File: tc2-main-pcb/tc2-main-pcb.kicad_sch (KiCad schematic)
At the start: 70 parts, among them J3 Conn_02x04_Odd_Even, SW2 K2-6639SP-M4SC-04, U1 ATtiny1616-M, U2 W25Q128JVS, U3 RP2040, U4 MT29F2G01ABAGDWB-IT, U5 SHT30-DIS, U6 PCF8563T, Y1 Crystal_GND24, Y2 Crystal

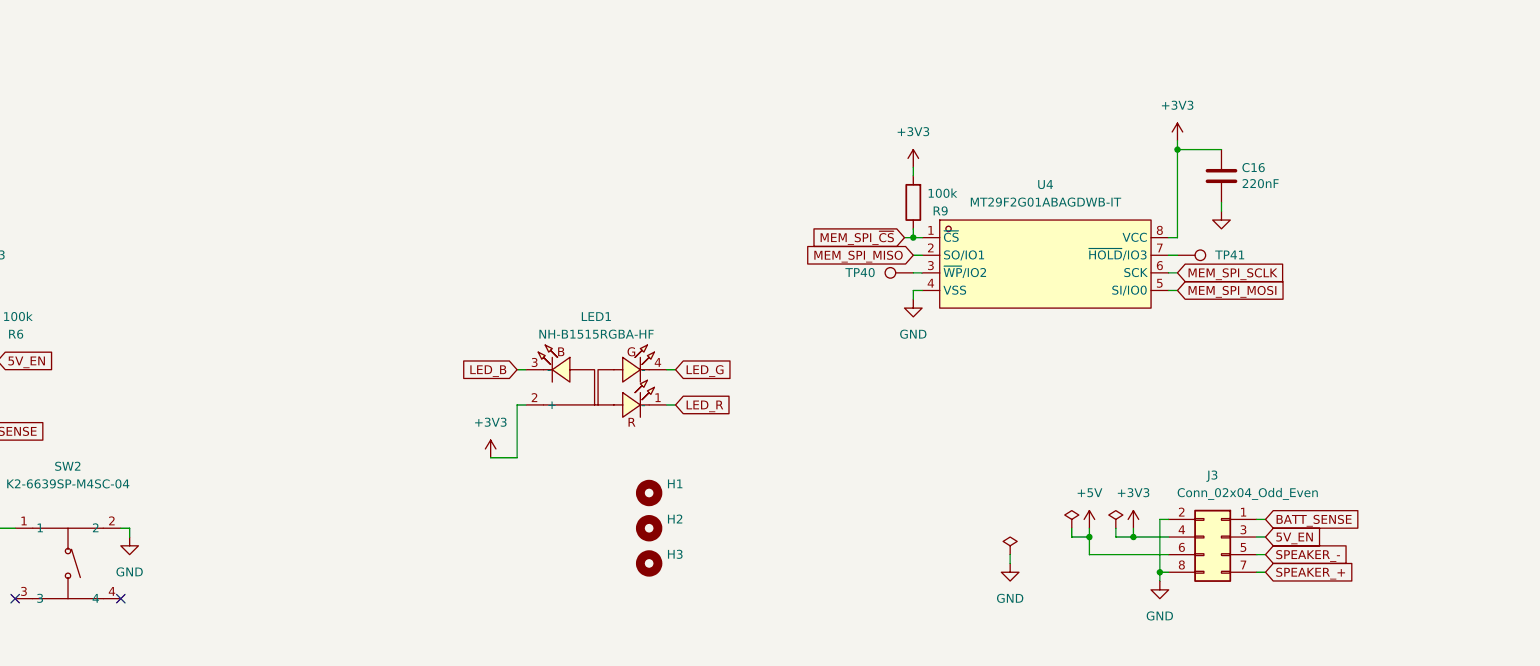
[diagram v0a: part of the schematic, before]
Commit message: Clean up of files and updated drawings for PCBs
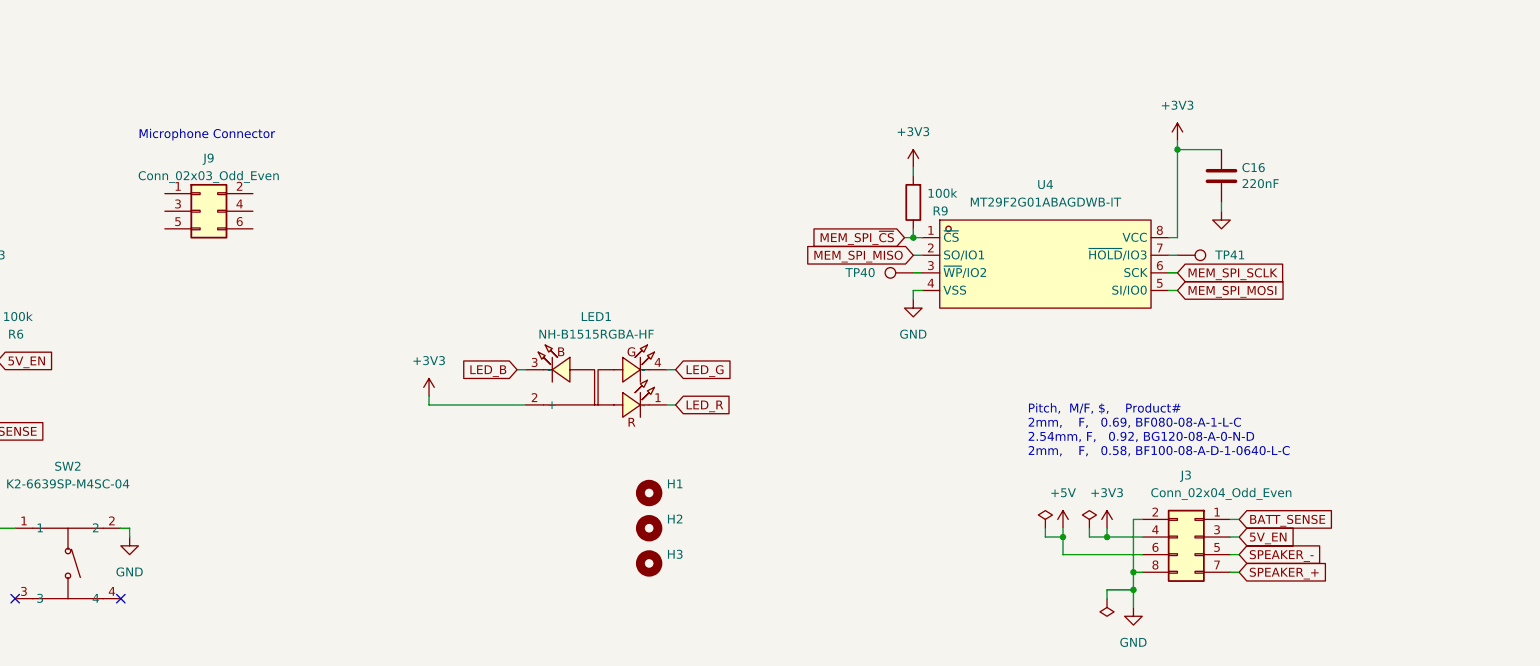
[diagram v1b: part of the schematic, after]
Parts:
- added J9: Conn_02x03_Odd_Even, cacophony-library:mic-pcb, symbol Connector_Generic:Conn_02x03_Odd_Even
- J3: footprint cacophony-library:power-pcb -> cacophony-library:power-pcb-3; Digikey (none) -> BF100-08-A-D-1-0640-L-C
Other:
- note added: "Microphone Connector"
- note added: "Pitch, M/F, $, Product# 2mm, F, 0.69, BF080-08-A-1-L-C 2.54mm, F, 0.92, BG120-08-A-0-N-D 2mm, F, 0.58, BF100-08-A-D-1-0640-L-C"
- moved on the sheet: J3

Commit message: Version 2 WIP
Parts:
- removed TP10, TP11, TP4: TestPoint, cacophony-library:TP, symbol Connector:TestPoint
- added H4: MountingHole, cacophony-library:Mouning_Hole_M3, symbol Mechanical:MountingHole
- added H5, H6: MountingHole, MountingHole:MountingHole_2.2mm_M2, symbol Mechanical:MountingHole
- added R34: 22ohm, Resistor_SMD:R_0402_1005Metric, symbol Device:R
- added R35: 100k, Resistor_SMD:R_0402_1005Metric, symbol Device:R
- added TP18, TP19, TP20: TestPoint, cacophony-library:TP, symbol Connector:TestPoint
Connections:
- net +3V3: now also J9.4 (Pin_4), R35.1
- net BATT_SENSE: now also U1.9 (PB5); no longer U1.15 (PC0)
- net GND: now also J9.2 (Pin_2), J9.3 (Pin_3), J9.6 (Pin_6), TP14.1, TP18.1, TP19.1, TP20.1
- net LEPTON_CLK_EN: now also U3.39 (GPIO27_ADC1); no longer U3.41 (GPIO29_ADC3)
- net LEPTON_PWR_DWN_L: now also U3.40 (GPIO28_ADC2); no longer U3.39 (GPIO27_ADC1)
- net LEPTON_RESET_L: now also U3.41 (GPIO29_ADC3); no longer U3.40 (GPIO28_ADC2)
- net RTC_BT_SENSE: now also U1.10 (PB4); no longer U1.7 (PA6)
- net SPEAKER_+: now also J3.5 (Pin_5); no longer J3.7 (Pin_7)
- net SPEAKER_-: now also J3.7 (Pin_7); no longer J3.5 (Pin_5)
- net at R3.1: now also U1.5 (PA4); no longer U1.2 (PA3)
- net at TP6.1: now also U1.8 (PA7); no longer U1.10 (PB4)
- net ~{WAKEUP_PING}: now reaches U1.12 (PB2)
- net ~{WAKEUP_PING}: now also U3.6 (GPIO4), R35.2
- net at R4.1: now also U1.2 (PA3); no longer U1.5 (PA4)
- net at SW2.1: now also U1.7 (PA6); no longer U1.8 (PA7)
- net at TP7.1: now also U1.15 (PC0); no longer U1.9 (PB5)
- net GPIO16: now reaches TP26.1, U3.27 (GPIO16)
- net GPIO3: now reaches TP13.1, U3.5 (GPIO3)
- net PDM_DATA: now reaches U3.2 (GPIO0)
- net PDM_DATA: now also J9.5 (Pin_5)
- net GPIO17: now reaches TP27.1, U3.28 (GPIO17)
- net PDM_CLOCK_: now reaches U3.3 (GPIO1)
- net PDM_CLOCK_: now also R34.1
- net PDM_CLOCK: now reaches J9.1 (Pin_1)
- net PDM_CLOCK: now also R34.2
- net GPIO2: now reaches TP12.1, U3.4 (GPIO2)
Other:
- note added: "TODO Add wakeup pin connecting ATtiny, RP2040, and RPi pulled up to 3.3V. Add wake up pin from ATtiny to RP2040."
- note added: "Test ground points."
- note removed: "Replace ATTiny, RTC with STM32 and Touch sensor"
- moved on the sheet: J9, R3, R4, SW2, TP12, TP13, TP26, TP27, TP6, TP7

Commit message: Thermal camera V2 WIP
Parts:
- J3: LCSC C124386 -> (none)
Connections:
- net SPEAKER_+: now also J3.7 (Pin_7); no longer J3.5 (Pin_5)
- net SPEAKER_-: now also J3.5 (Pin_5); no longer J3.7 (Pin_7)
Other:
- note added: "Pitch, M/F, $, Product# 2mm, F, 0.69, BF080-08-A-1-L-C 2.54mm, F, 0.92, BG120-08-A-0-N-D 2mm, F, 0.58, BF100-08-A-D-1-0640-L-C Old part C124386"
- note removed: "Pitch, M/F, $, Product# 2mm, F, 0.69, BF080-08-A-1-L-C 2.54mm, F, 0.92, BG120-08-A-0-N-D 2mm, F, 0.58, BF100-08-A-D-1-0640-L-C"
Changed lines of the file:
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@@
     (effects (font (size 1.27 1.27)) (justify left bottom))
   )
-  (text "Pitch,  M/F, $,    Product#\n2mm,    F,   0.69, BF080-08-A-1-L-C\n2.54mm, F,   0.92, BG120-08-A-0-N-D\n2mm,    F,   0.58, BF100-08-A-D-1-0640-L-C\n"
+  (text "Pitch,  M/F, $,    Product#\n2mm,    F,   0.69, BF080-08-A-1-L-C\n2.54mm, F,   0.92, BG120-08-A-0-N-D\n2mm,    F,   0.58, BF100-08-A-D-1-0640-L-C\n\nOld part C124386\n"
     (at 242.57 254 0)
     (effects (font (face "RobotoMono Nerd Font Mono") (size 1.27 1.27)) (justify left bottom))
@@
     )
   )
-  (global_label "SPEAKER_-" (shape input) (at 273.05 270.51 0) (fields_autoplaced)
+  (global_label "SPEAKER_-" (shape input) (at 273.05 267.97 0) (fields_autoplaced)
     (effects (font (size 1.27 1.27)) (justify left))
-    (property "Intersheetrefs" "${INTERSHEET_REFS}" (at 286.4093 270.4306 0)
+    (property "Intersheetrefs" "${INTERSHEET_REFS}" (at 286.4093 267.8906 0)
       (effects (font (size 1.27 1.27)) (justify left) hide)
     )
@@
     )
   )
-  (global_label "SPEAKER_+" (shape input) (at 273.05 267.97 0) (fields_autoplaced)
+  (global_label "SPEAKER_+" (shape input) (at 273.05 270.51 0) (fields_autoplaced)
     (effects (font (size 1.27 1.27)) (justify left))
-    (property "Intersheetrefs" "${INTERSHEET_REFS}" (at 286.4093 267.8906 0)
+    (property "Intersheetrefs" "${INTERSHEET_REFS}" (at 286.4093 270.4306 0)
       (effects (font (size 1.27 1.27)) (justify left) hide)
     )
@@
       (effects (font (size 1.27 1.27)) hide)
     )
-    (property "LCSC" "C124386" (at 266.7 265.43 0)
+    (property "LCSC" "" (at 266.7 265.43 0)
       (effects (font (size 1.27 1.27)) hide)
     )

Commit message: P2 milestone
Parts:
- removed C17: 220nF, Capacitor_SMD:C_0402_1005Metric, symbol Device:C_Small
- removed H2: MountingHole, cacophony-library:Mouning_Hole_M3, symbol Mechanical:MountingHole
- removed J3: Conn_02x04_Odd_Even, cacophony-library:power-pcb-3, symbol Connector_Generic:Conn_02x04_Odd_Even
- removed TP15, TP16, TP2, TP3, TP44, TP5, TP6, TP7, TP8: TestPoint, cacophony-library:TP, symbol Connector:TestPoint
- removed U5: SHT30-DIS, Sensor_Humidity:Sensirion_DFN-8-1EP_2.5x2.5mm_P0.5mm_EP1.1x1.7mm, symbol Sensor_Humidity:SHT30-DIS
- added C17: 1u, Capacitor_SMD:C_0402_1005Metric, symbol Device:C
- added C38, C39, C43: 10uF, Capacitor_SMD:C_0603_1608Metric, symbol Device:C_Small
- added J10: Conn_02x06_Odd_Even, cacophony-library:power-pcb-3.1, symbol Connector_Generic:Conn_02x06_Odd_Even
- added J2: Conn_01x03, Connector_PinHeader_2.54mm:PinHeader_1x03_P2.54mm_Vertical, symbol Connector_Generic:Conn_01x03
- added J3: Conn_01x03, cacophony-library:JST_SH_BM03B-SRSS-TB_1x03-1MP_P1.00mm_Vertical, symbol cacophony-library:Conn_01x03_MP
- added Q1: Q_PMOS_GSD, Package_TO_SOT_SMD:SOT-23, symbol Device:Q_PMOS_GSD
- added R15, R38: 100k, Resistor_SMD:R_0402_1005Metric, symbol Device:R
- added R39: 180R, Resistor_SMD:R_0402_1005Metric, symbol Device:R
- added TP28, TP6: TestPoint_2Pole, cacophony-library:test-point-2p, symbol Connector:TestPoint_2Pole
- added U13: AHT21, cacophony-library:SENSOR-SMD_L3.0-W3.0-P1.00-BR, symbol cacophony-library:AHT21
- H1, H3, H4, H5, H6, TP1, TP12, TP13, TP14, TP17, TP18, TP19, TP20, TP26, TP27, TP40, TP41, TP46, TP47, TP9: now left out of the parts list
- SW2: footprint cacophony-library:KEY-SMD_4P-L6.0-W6.0-P3.90-LS9.0 -> cacophony-library:KEY-SMD_4P-L6.0-W6.0-P3.90_K2-6639SP-K4SC-04; symbol cacophony-library:K2-6639SP-M4SC-04 -> cacophony-library:K2-6639SP-O4SC-04; LCSC Part C149500 -> C223734
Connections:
- net +3V3: now also C17.1, C43.1, J10.3 (Pin_3), Q1.2 (S), R38.2, R39.1; no longer C10.1, C11.1, C12.1, C13.1, C14.1, C15.1, C16.1, C2.1, C8.1, C9.1, R2.1, R9.2, U2.8 (VCC), U3.1 (IOVDD), U3.10 (IOVDD), U3.22 (IOVDD), U3.33 (IOVDD), U3.42 (IOVDD), U3.43 (ADC_AVDD), U3.44 (VREG_IN), U3.48 (USB_VDD), U3.49 (IOVDD), U4.8 (VCC)
- net +5V: now also J10.5 (Pin_5), TP28.2
- net 5V_EN: now also J10.4 (Pin_4)
- net BATT_SENSE: now also J10.2 (Pin_2)
- net GND: now also SW2.4, C17.2, C38.2, C39.2, C43.2, J10.1 (Pin_1), J10.7 (Pin_7), J2.2 (Pin_2), J3.2 (Pin_2), TP28.1, TP6.1, U13.5 (GND); no longer SW2.2
- net SCL: now also U13.3 (SCL)
- net SDA: now also U13.4 (SDA)
- net SPEAKER_+: now also J10.6 (Pin_6)
- net SPEAKER_-: now also J10.8 (Pin_8)
- net SWD: now also J2.3 (Pin_3), J3.3 (Pin_3)
- net SW_CLK: now also J2.1 (Pin_1), J3.1 (Pin_1)
- net ~{WAKEUP_PING}: now also U1.15 (PC0); no longer U1.12 (PB2)
- net ~{EN_RP2040_POWER}: now reaches U1.20 (PA1)
- net ~{EN_RP2040_POWER}: now also Q1.1 (G), R38.1
- net at TP1.1: now also U1.18 (PC3); no longer U1.17 (PC2)
- net ATTINY_RX: now reaches U1.11 (PB3)
- net ~{PI_SHUTDOWN}: now reaches U1.8 (PA7)
- new net: R15.2, U1.12 (PB2)
- new net: C39.1, R39.2, U13.2 (VDD)
- new net +3V3_rp2040: C10.1, C11.1, C12.1, C13.1, C14.1, C15.1, C16.1, C2.1, C38.1, C8.1, C9.1, Q1.3 (D), R2.1, R9.2, TP6.2, U2.8 (VCC), U3.1 (IOVDD), U3.10 (IOVDD), U3.22 (IOVDD), U3.33 (IOVDD), U3.42 (IOVDD), U3.43 (ADC_AVDD), U3.44 (VREG_IN), U3.48 (USB_VDD), U3.49 (IOVDD), U4.8 (VCC)
- new net ATTINY_TX: R15.1
- new net EN_PERIPH_POWER: J10.11 (Pin_11), U1.17 (PC2)
- new net OUT_RX: J10.12 (Pin_12)
- new net OUT_TX: J10.10 (Pin_10)
- no-connect marks 2 -> 7
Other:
- note added: "C160389"
- note removed: "TODO Add wakeup pin connecting ATtiny, RP2040, and RPi pulled up to 3.3V. Add wake up pin from ATtiny to RP2040."
- moved on the sheet: C16, H5, H6, J9, R10, R11, R35, R6, R9, TP14, TP18, TP19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

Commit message: P3-Nov release
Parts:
- removed C1: 220nF, Capacitor_SMD:C_0402_1005Metric, symbol Device:C_Small
- removed J2: Conn_01x03, Connector_PinHeader_2.54mm:PinHeader_1x03_P2.54mm_Vertical, symbol Connector_Generic:Conn_01x03
- removed LED1: NH-B1515RGBA-HF, cacophony-library:LED-ARRAY-SMD_4P-L1.6-W1.5-TL_NH-B1515RGBA, symbol cacophony-library:NH-B1515RGBA-HF
- removed R15, R35, R6: 100k, Resistor_SMD:R_0402_1005Metric, symbol Device:R
- removed R3, R4, R5: 180R, Resistor_SMD:R_0402_1005Metric, symbol Device:R
- removed SW2: K2-6639SP-M4SC-04, cacophony-library:KEY-SMD_4P-L6.0-W6.0-P3.90_K2-6639SP-K4SC-04, symbol cacophony-library:K2-6639SP-O4SC-04
- removed TP1: TestPoint, cacophony-library:TP, symbol Connector:TestPoint
- removed TP28, TP6: TestPoint_2Pole, cacophony-library:test-point-2p, symbol Connector:TestPoint_2Pole
- removed U1: ATtiny1616-M, Package_DFN_QFN:VQFN-20-1EP_3x3mm_P0.4mm_EP1.7x1.7mm, symbol MCU_Microchip_ATtiny:ATtiny1616-M
- added C33 (x4): 22uF, Capacitor_SMD:C_0603_1608Metric, symbol Device:C_Small
- added C48: 220nF, Capacitor_SMD:C_0402_1005Metric, symbol Device:C_Small
- added TP10, TP3, TP6: TP_2P, cacophony-library:test-point-2p, symbol cacophony-library:TestPoint_2Pole
- added U16: M24C02-WMN, Package_SO:SOIC-8_3.9x4.9mm_P1.27mm, symbol Memory_EEPROM:M24C02-WMN
- H1, H3, H4: footprint cacophony-library:Mouning_Hole_M3 -> cacophony-library:MountingHole_3.2mm_M3
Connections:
- net BATT_SENSE is gone; now on net OUT_RX: J10.2 (Pin_2)
- net +3V3: now also J10.10 (Pin_10), C33.1, C33.1, C48.2, TP6.2, U16.8 (VCC); no longer J10.3 (Pin_3)
- net +3V3_rp2040: now also TP3.2
- net +5V: now also J10.8 (Pin_8), C33.1, C33.1, TP10.2; no longer J10.5 (Pin_5)
- net 5V_EN: now also J10.1 (Pin_1); no longer J10.4 (Pin_4)
- net GND: now also J10.12 (Pin_12), J10.6 (Pin_6), C33.2, C33.2, C33.2, C33.2, C48.1, TP10.1, TP3.1, TP6.1, U16.4 (VSS); no longer J10.1 (Pin_1), J10.7 (Pin_7)
- net OUT_RX: no longer J10.12 (Pin_12)
- net OUT_TX: now also J10.4 (Pin_4); no longer J10.10 (Pin_10)
- net SCL: now also U16.5 (SDA)
- net SDA: now also U16.6 (SCL)
- net SPEAKER_+: now also J10.9 (Pin_9); no longer J10.6 (Pin_6)
- net SPEAKER_-: now also J10.7 (Pin_7); no longer J10.8 (Pin_8)
- net RTC_OSCO: now reaches U6.2 (OSCO), Y2.1
- net RTC_OSCI: now reaches U6.1 (OSCI), Y2.2
- net RTC_VDD: now reaches C18.1, D3.1 (K), R8.1, U6.8 (VDD)
- net RTC_BATTERY: now reaches BT1.1 (+), R7.1, R8.2
- net RTC_CLKO: now reaches TP17.1, U6.7 (CLKO)
- net AHT21_VDD: now reaches C39.1, R39.2, U13.2 (VDD)
- net MEM_~{WP}/IO2: now reaches TP40.1, U4.3 (~{WP}/IO2)
- net MEM_~{HOLD}/IO3: now reaches TP41.1, U4.7 (~{HOLD}/IO3)
- net PDM_CLOCK_ renamed PDM_CLOCK_PHY
- net RTC_BT_SENSE renamed RTC_BT_SENSE_PHY
- net ~{WAKEUP_PING} renamed ~{READ_ATTINY_CMD_REG}
- new net BATT_SENSE_HV: J10.3 (Pin_3)
- new net BATT_SENSE_LV: J10.5 (Pin_5)
- no-connect marks 7 -> 8
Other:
- added sheet ATtiny1616 (attiny1616.kicad_sch)
- note added: "Always double check allignemnt with plug PCB"
- moved on the sheet: BT1, C18, D2, D3, H1, H3, H4, J10, R34, R7, R8, TP12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

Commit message: v0.4.0
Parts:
- removed TP13, TP46, TP47, TP9: TestPoint, cacophony-library:TP, symbol Connector:TestPoint
- added C61, C63: 22pF, Capacitor_SMD:C_0402_1005Metric, symbol Device:C_Small
- added H2: MountingHole, cacophony-library:MountingHole_3.2mm_M3, symbol Mechanical:MountingHole
- added J12: USB_B_Micro, cacophony-library:MICRO-USB-TH_MICRO-USB-A14, symbol Connector:USB_B_Micro
- added R48, R50, R51: 22ohm, Resistor_SMD:R_0402_1005Metric, symbol Device:R
- added TP13: TP_2P, cacophony-library:test-point-2p, symbol cacophony-library:TestPoint_2Pole
- C62, C64, C65, C66: renamed from C33; LCSC C2980159 -> C86295
- H5, H6: footprint MountingHole:MountingHole_2.2mm_M2 -> cacophony-library:MountingHole_2.2mm_M2
- J10: LCSC (none) -> C6470934
- TP10, TP3, TP6: now left out of the parts list
- U13: value AHT21 -> AHT20_C2757850; symbol cacophony-library:AHT21 -> cacophony-library:AHT20_C2757850; LCSC (none) -> C2757850; LCSC Part C2827328 -> (none)
- U4: LCSC (none) -> C410863; LCSC Part C410863 -> (none)
- U6: footprint Package_SO:SOIC-8_3.9x4.9mm_P1.27mm -> cacophony-library:SOIC-8_3.9x4.9mm_P1.27mm
- renumbered R34 to R28
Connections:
- net GND: now also C61.2, C63.2, J12.5 (GND), J12.6 (Shield), TP13.1
- net RPI_SPI_MISO: now also R48.2; no longer U3.18 (GPIO15)
- net RTC_BATTERY: now also TP13.2
- net RTC_OSCI: now also C63.1
- net RTC_OSCO: now also C61.1
- net SCL: now also U16.6 (SCL); no longer U16.5 (SDA)
- net SDA: now also U16.5 (SDA); no longer U16.6 (SCL)
- net USB_D+: now also J12.3 (D+), R50.2; no longer U3.47 (USB_DP)
- net USB_D-: now also J12.2 (D-), R51.2; no longer U3.46 (USB_DM)
- net GPIO3 renamed I2C_BUS_LOCK
- new net RPI_SPI_MISO_PHY: R48.1, U3.18 (GPIO15)
- new net USB_D+_PHY: R50.1, U3.47 (USB_DP)
- new net USB_D-_PHY: R51.1, U3.46 (USB_DM)
- no-connect marks 8 -> 10
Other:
- note added: "I2C Address 0x38"
- note added: "I2C Address 0x51"
- note removed: "Pitch, M/F, $, Product# 2mm, F, 0.69, BF080-08-A-1-L-C 2.54mm, F, 0.92, BG120-08-A-0-N-D 2mm, F, 0.58, BF100-08-A-D-1-0640-L-C Old part C124386"
- moved on the sheet: BT1, C48, D2, R28, R7, TP26, TP27, U16

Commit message: Small update for v0.4.1
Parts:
- added R53: 1k, Resistor_SMD:R_0402_1005Metric, symbol Device:R
- BT1: LCSC (none) -> C80909
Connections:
- net I2C_BUS_LOCK: now also R53.1; no longer U3.5 (GPIO3)
- new net I2C_BUS_LOCK_PHY: R53.2, U3.5 (GPIO3)
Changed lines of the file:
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@@
 	(wire
 		(pts
+			(xy 240.03 96.52) (xy 246.38 96.52)
+		)
+		(stroke
+			(width 0)
+			(type default)
+		)
+	)
+	(wire
+		(pts
 			(xy 125.73 260.35) (xy 125.73 261.62)
 		)
@@
 	(wire
 		(pts
-			(xy 207.01 93.98) (xy 231.14 93.98)
+			(xy 207.01 93.98) (xy 215.9 93.98)
 		)
 		(stroke
@@
 	(wire
 		(pts
-			(xy 207.01 96.52) (xy 246.38 96.52)
+			(xy 207.01 96.52) (xy 232.41 96.52)
 		)
 		(stroke
@@
 		)
 	)
+	(label "I2C_BUS_LOCK_PHY"
+		(at 208.28 96.52 0)
+		(fields_autoplaced yes)
+		(effects
+			(font
+				(size 1.27 1.27)
+			)
+			(justify left bottom)
+		)
+	)
 	(label "PDM_CLOCK_PHY"
 		(at 208.28 91.44 0)
@@
 	)
 	(symbol
+		(lib_id "Device:R")
+		(at 236.22 96.52 270)
+		(unit 1)
+		(exclude_from_sim no)
+		(in_bom yes)
+		(on_board yes)
+		(dnp no)
+		(property "Reference" "R53"
+			(at 231.14 95.25 90)
+			(effects
+				(font
+					(size 1.27 1.27)
+				)
+			)
+		)
+		(property "Value" "1k"
+			(at 241.3 95.25 90)
+			(effects
+				(font
+					(size 1.27 1.27)
+				)
+			)
+		)
+		(property "Footprint" "Resistor_SMD:R_0402_1005Metric"
+			(at 236.22 94.742 90)
+			(effects
+				(font
+					(size 1.27 1.27)
+				)
+				(hide yes)
+			)
+		)
+		(property "Datasheet" "~"
+			(at 236.22 96.52 0)
+			(effects
+				(font
+					(size 1.27 1.27)
+				)
+				(hide yes)
+			)
+		)
+		(property "Description" ""
+			(at 236.22 96.52 0)
+			(effects
+				(font
+					(size 1.27 1.27)
+				)
+				(hide yes)
+			)
+		)
+		(property "JLCPCB" ""
+			(at 236.22 96.52 0)
+			(effects
+				(font
+					(size 1.27 1.27)
+				)
+				(hide yes)
+			)
+		)
+		(property "LCSC" "C11702"
+			(at 236.22 96.52 0)
+			(effects
+				(font
+					(size 1.27 1.27)
+				)
+				(hide yes)
+			)
+		)
+		(pin "1"
+		)
+		(pin "2"
+		)
+		(instances
+			(project "tc2-main-pcb"
+				(path "/0662f88c-5300-4b75-bef3-048a3227af84"
+					(reference "R53")
+					(unit 1)
+				)
+			)
+		)
+	)
+	(symbol
 		(lib_id "power:GND")
 		(at 203.2 237.49 0)
@@
 			)
 		)
+		(property "LCSC" "C80909"
+			(at 317.5 232.41 0)
+			(effects
+				(font
+					(size 1.27 1.27)
+				)
+				(hide yes)
+			)
+		)
 		(pin "1"
 		)
@@
 	(symbol
 		(lib_id "Connector:TestPoint")
-		(at 231.14 93.98 270)
+		(at 215.9 93.98 270)
 		(unit 1)
 		(exclude_from_sim no)
@@
 		(dnp no)
 		(property "Reference" "TP12"
-			(at 238.76 93.98 90)
+			(at 223.52 93.98 90)
 			(effects
 				(font
 					(size 1.27 1.27)
 				)
+				(hide yes)
 			)
 		)
 		(property "Value" "TestPoint"
-			(at 233.1721 96.52 0)
+			(at 217.9321 96.52 0)
 			(effects
 				(font
@@
 		)
 		(property "Footprint" "cacophony-library:TP"
-			(at 231.14 99.06 0)
+			(at 215.9 99.06 0)
 			(effects
 				(font
@@
 		)
 		(property "Datasheet" "~"
-			(at 231.14 99.06 0)
+			(at 215.9 99.06 0)
 			(effects
 				(font
@@
 		)
 		(property "Description" ""
-			(at 231.14 93.98 0)
+			(at 215.9 93.98 0)
 			(effects
 				(font

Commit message: panelize WIP
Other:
- note added: "EEPROM 2K"
- note added: "I2C Address 0x50"
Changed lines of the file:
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@@
+		)
+	)
+	(text "EEPROM 2K"
+		(exclude_from_sim no)
+		(at 199.39 220.98 0)
+		(effects
+			(font
+				(size 2 2)
+			)
+			(justify left bottom)
+		)
+	)
+	(text "I2C Address 0x50"
+		(exclude_from_sim no)
+		(at 213.36 233.68 0)
+		(effects
+			(font
+				(size 1.27 1.27)
+			)
+			(justify left bottom)
 		)
 	)
